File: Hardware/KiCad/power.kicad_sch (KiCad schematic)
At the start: 38 parts, among them U6 TP6841S6, U7 TPS73233

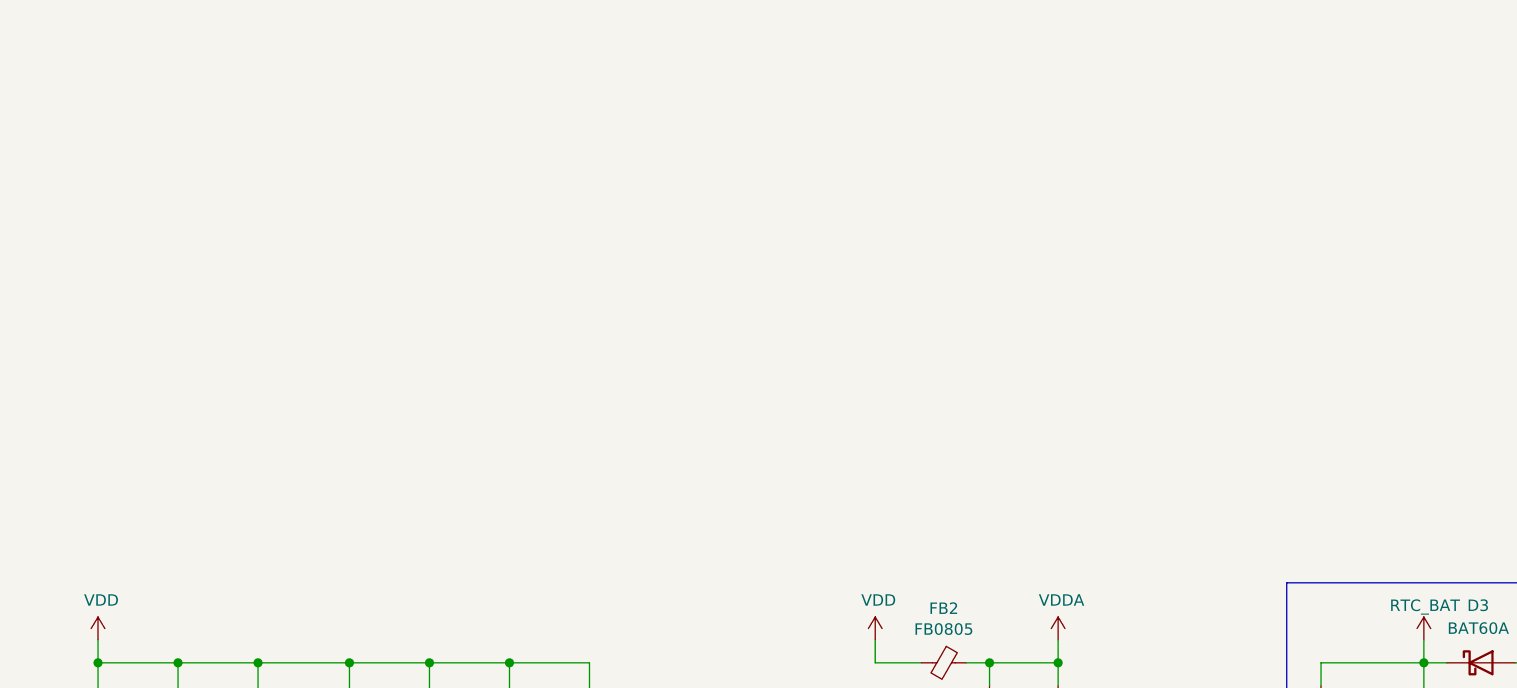
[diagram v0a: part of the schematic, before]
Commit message: Added footprints for decoupling caps
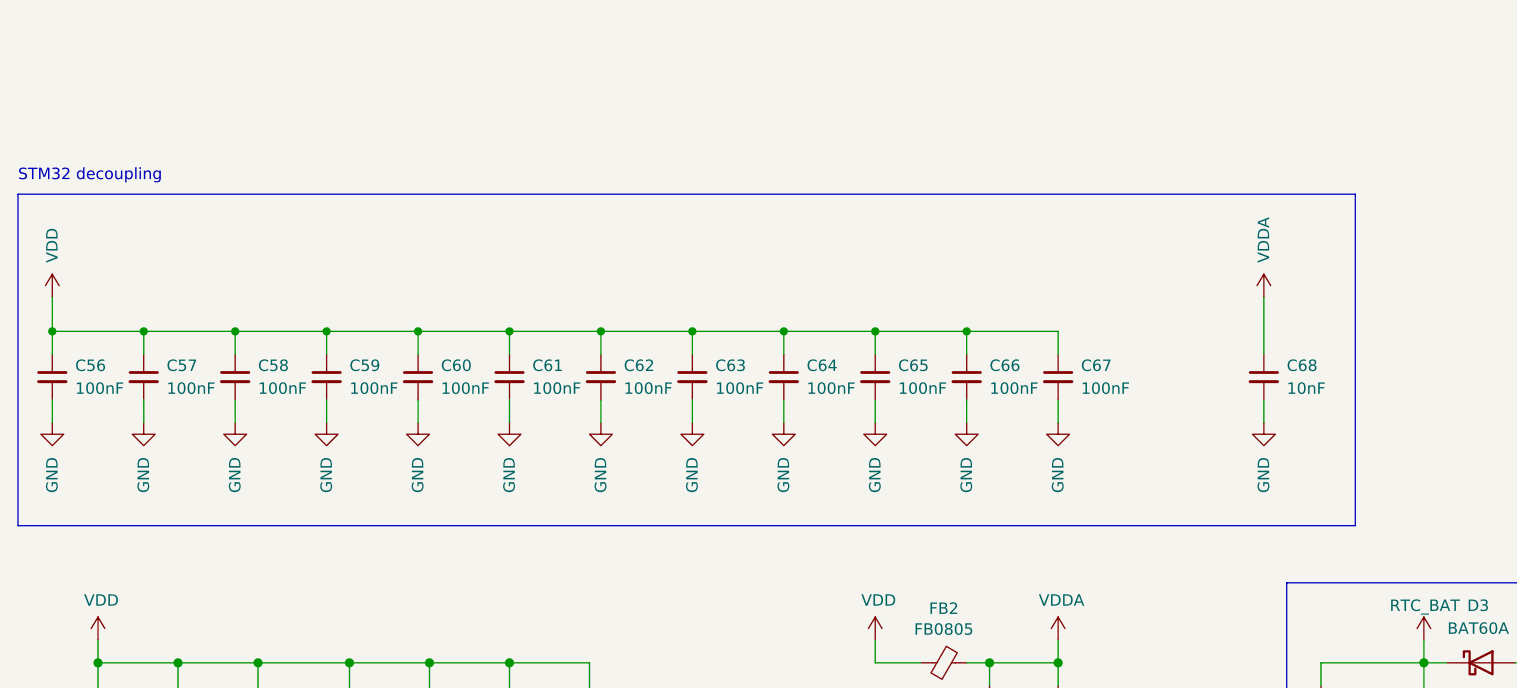
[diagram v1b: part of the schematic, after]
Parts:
- added C56, C57, C58, C59, C60, C61, C62, C63, C64, C65, C66, C67: 100nF, Capacitor_SMD:C_0402_1005Metric, symbol Device:C_Small
- added C68: 10nF, Capacitor_SMD:C_0402_1005Metric, symbol Device:C_Small
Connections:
- net GND: now also C56.2, C57.2, C58.2, C59.2, C60.2, C61.2, C62.2, C63.2, C64.2, C65.2, C66.2, C67.2, C68.2
- net VDD: now also C56.1, C57.1, C58.1, C59.1, C60.1, C61.1, C62.1, C63.1, C64.1, C65.1, C66.1, C67.1
- net VDDA: now also C68.1
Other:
- note added: "STM32 decoupling"

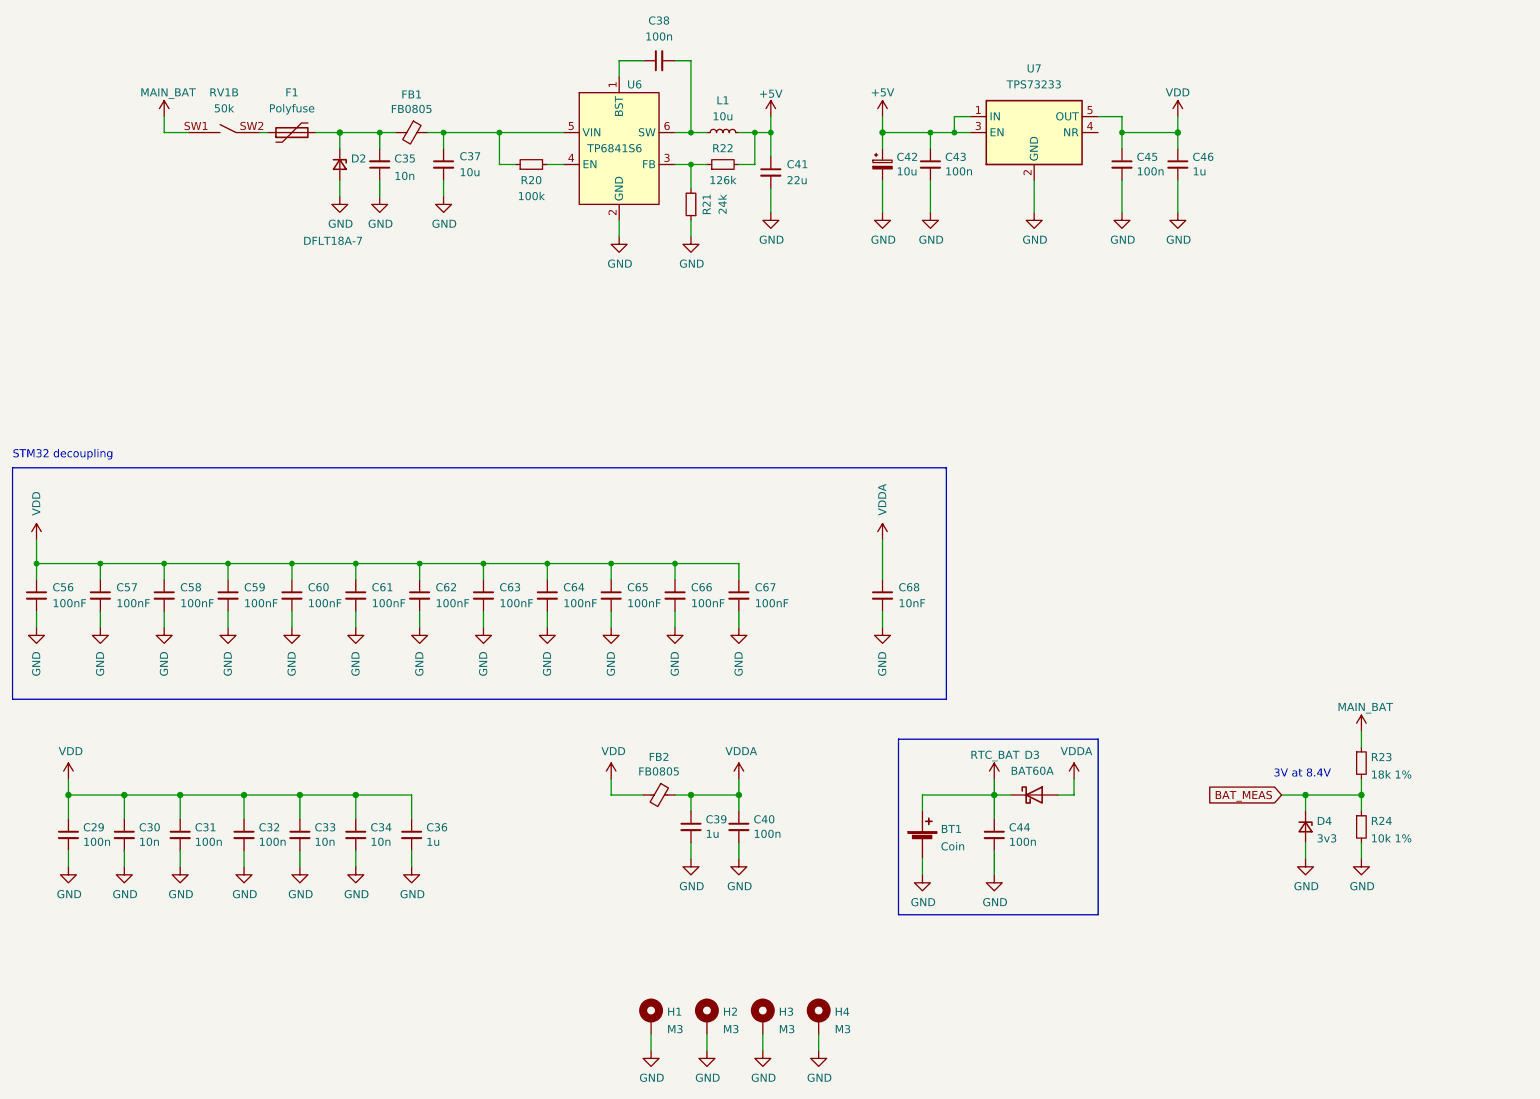
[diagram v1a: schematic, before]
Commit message: Update
- `H*` holes changed to M2
- RTC battery was connected to `VDDA` instead of `VDD`
- added CC1200 decoupling caps
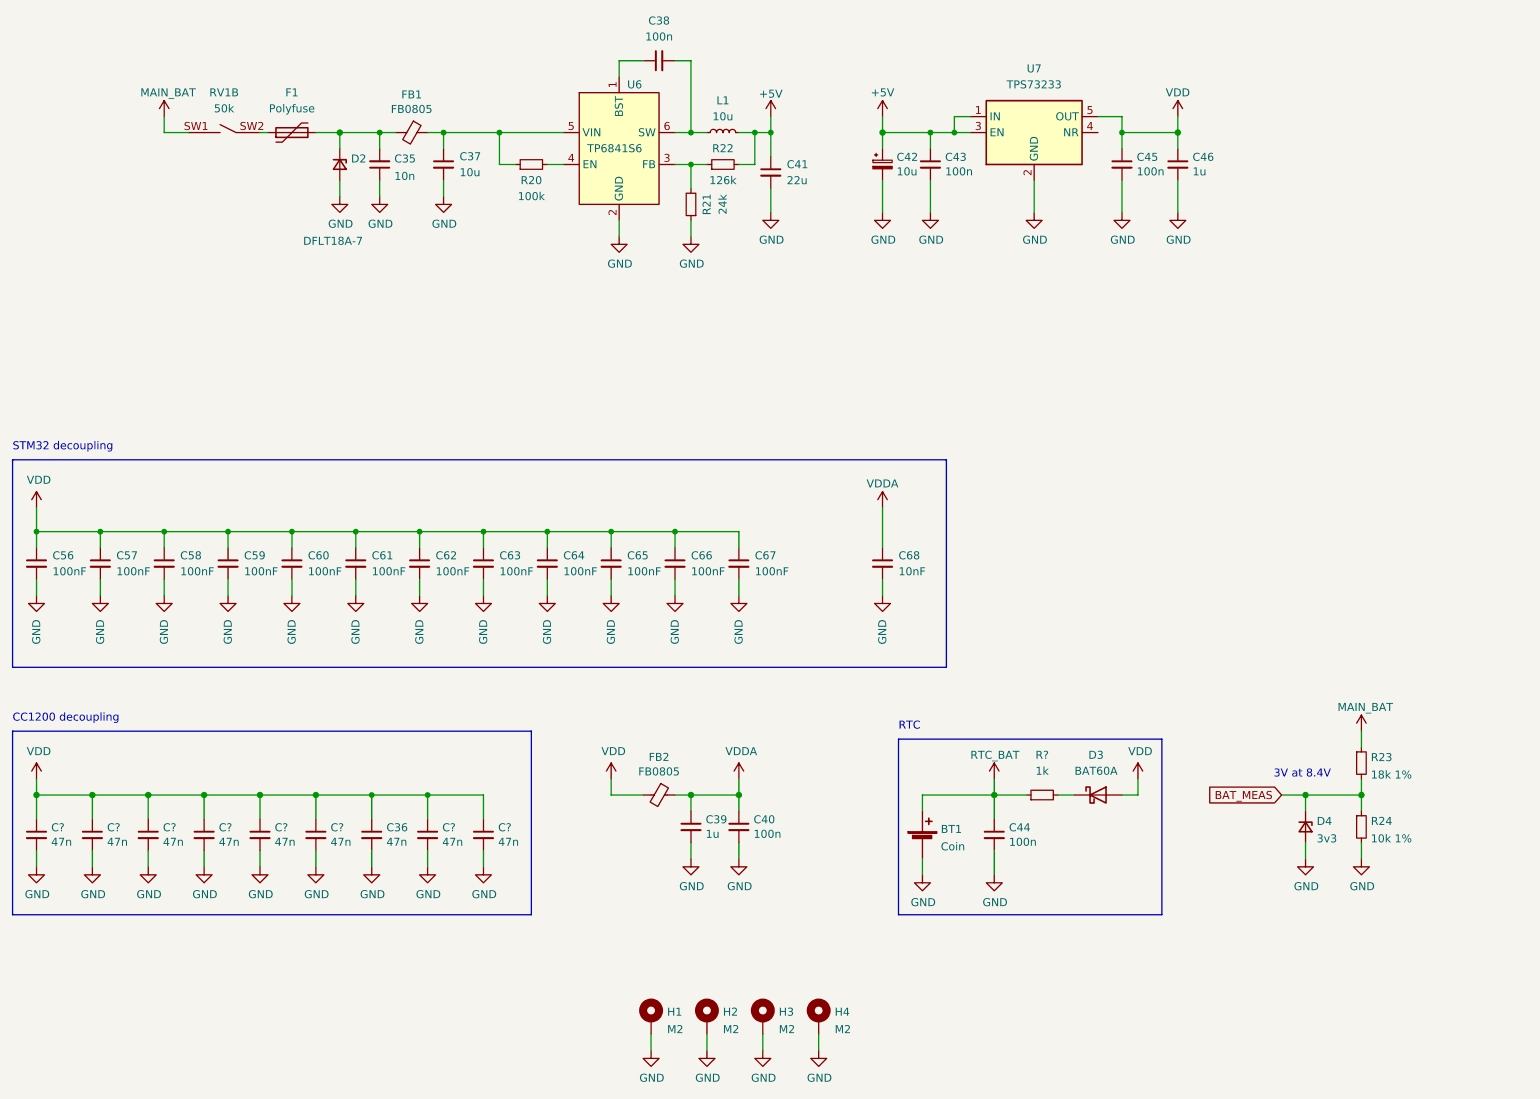
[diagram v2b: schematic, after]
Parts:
- removed C29, C31, C32: 100n, Capacitor_SMD:C_0402_1005Metric, symbol pkl_device:pkl_C_Small
- removed C30, C33, C34: 10n, Capacitor_SMD:C_0402_1005Metric, symbol pkl_device:pkl_C_Small
- added C? (x8): 47n, Capacitor_SMD:C_0402_1005Metric, symbol pkl_device:pkl_C_Small
- added R?: 1k, Resistor_SMD:R_0402_1005Metric, symbol pkl_device:pkl_R_Small
- C36: value 1u -> 47n
- H1, H2, H3, H4: value M3 -> M2; footprint MountingHole:MountingHole_2.7mm_M2.5_DIN965_Pad -> MountingHole:MountingHole_2.2mm_M2_DIN965_Pad
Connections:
- net GND: now also C?.2, C?.2, C?.2, C?.2, C?.2, C?.2, C?.2, C?.2
- net VBAT: now also R?.1; no longer D3.1 (K)
- net VDD: now also D3.2 (A), C?.1, C?.1, C?.1, C?.1, C?.1, C?.1, C?.1, C?.1
- net VDDA: no longer D3.2 (A)
- new net: D3.1 (K), R?.2
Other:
- note added: "CC1200 decoupling"
- note added: "RTC"
- moved on the sheet: C36, C56, C57, C58, C59, C60, C61, C62, C63, C64, C65, C66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

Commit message: adjust footprints
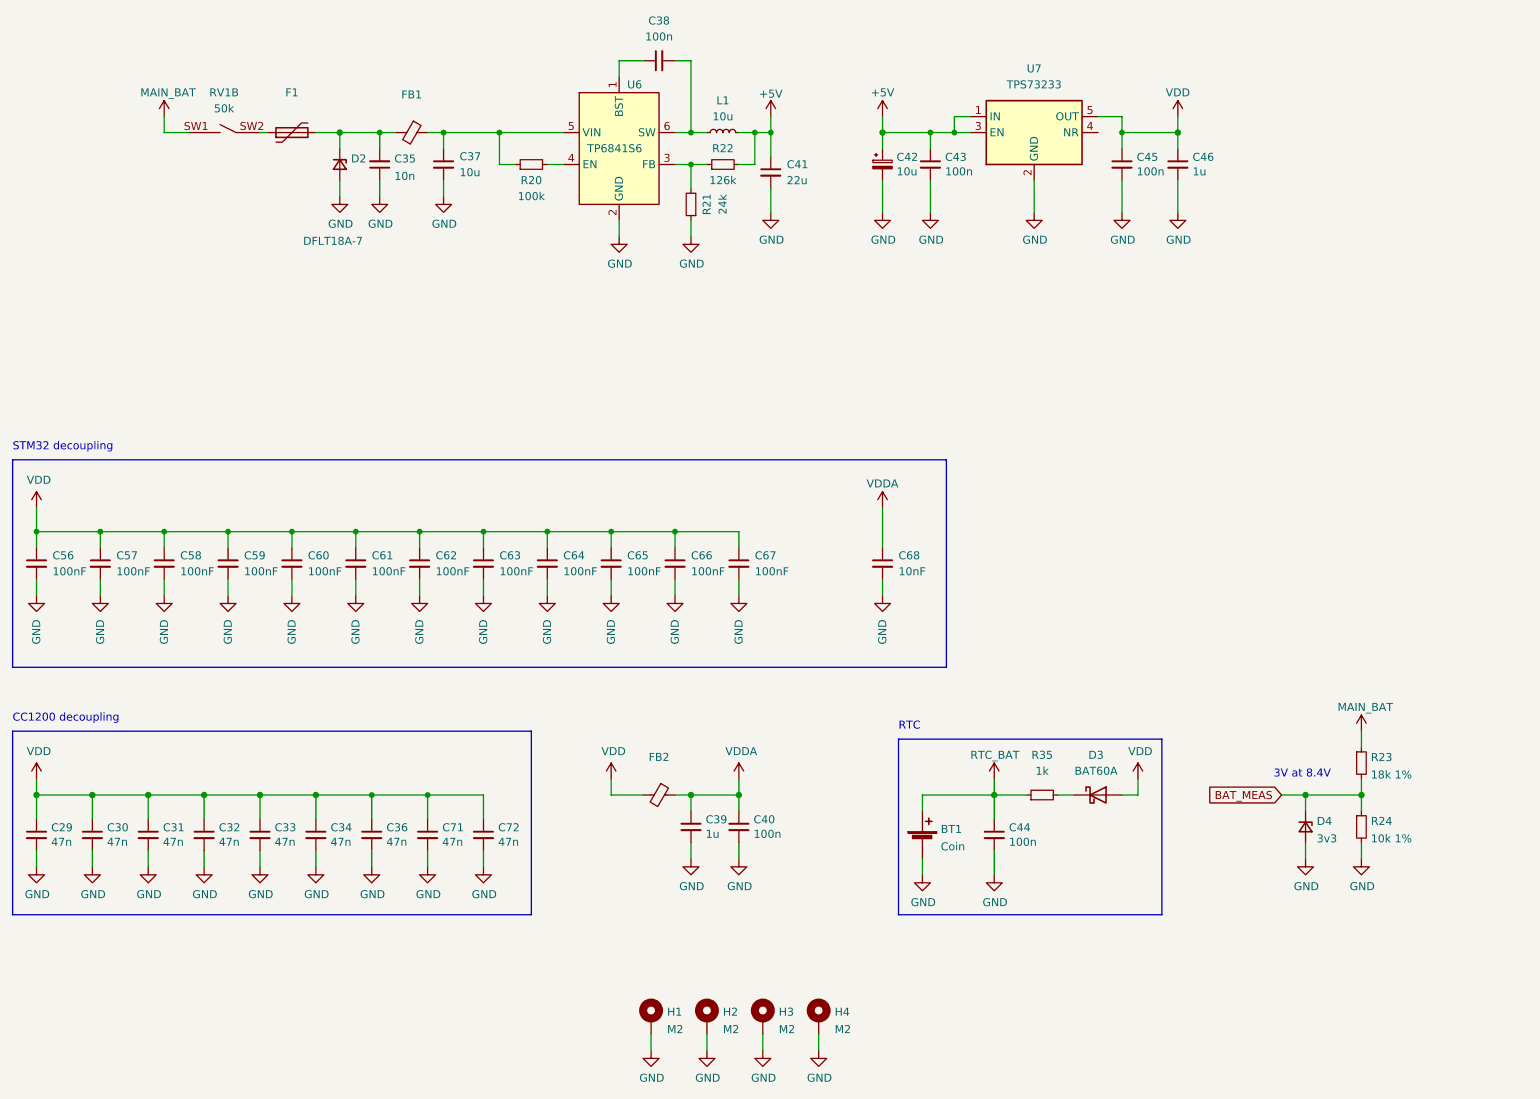
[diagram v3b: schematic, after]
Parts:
- F1: value Polyfuse -> (none); footprint Fuse:Fuse_0805_2012Metric -> (none)
- FB1, FB2: value FB0805 -> (none); footprint pkl_dipol:L_0805 -> (none)
- gave numbers to parts that had none: 9
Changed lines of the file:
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@@
   (symbol (lib_id "pkl_device:pkl_C_Small") (at 41.91 147.32 0) (unit 1)
     (in_bom yes) (on_board yes)
-    (property "Reference" "C?" (id 0) (at 44.2468 146.1516 0)
+    (property "Reference" "C30" (id 0) (at 44.2468 146.1516 0)
       (effects (font (size 1.27 1.27)) (justify left))
     )
@@
   (symbol (lib_id "pkl_device:pkl_C_Small") (at 50.8 147.32 0) (unit 1)
     (in_bom yes) (on_board yes)
-    (property "Reference" "C?" (id 0) (at 53.1368 146.1516 0)
+    (property "Reference" "C31" (id 0) (at 53.1368 146.1516 0)
       (effects (font (size 1.27 1.27)) (justify left))
     )
@@
   (symbol (lib_id "pkl_device:pkl_C_Small") (at 68.58 147.32 0) (unit 1)
     (in_bom yes) (on_board yes)
-    (property "Reference" "C?" (id 0) (at 70.9168 146.1516 0)
+    (property "Reference" "C33" (id 0) (at 70.9168 146.1516 0)
       (effects (font (size 1.27 1.27)) (justify left))
     )
@@
   (symbol (lib_id "power:GND") (at 104.14 152.4 0) (unit 1)
     (in_bom yes) (on_board yes)
-    (property "Reference" "#PWR?" (id 0) (at 104.14 158.75 0)
+    (property "Reference" "#PWR0208" (id 0) (at 104.14 158.75 0)
       (effects (font (size 1.27 1.27)) hide)
     )
@@
     (in_bom yes) (on_board yes)
     (property "Reference" "FB1" (id 0) (at 92.71 29.5402 90))
-    (property "Value" "FB0805" (id 1) (at 92.71 31.8516 90))
-    (property "Footprint" "pkl_dipol:L_0805" (id 2) (at 92.71 33.782 90)
+    (property "Value" "" (id 1) (at 92.71 31.8516 90))
+    (property "Footprint" "" (id 2) (at 92.71 33.782 90)
       (effects (font (size 1.27 1.27)) hide)
     )
@@
   (symbol (lib_id "pkl_device:pkl_C_Small") (at 77.47 147.32 0) (unit 1)
     (in_bom yes) (on_board yes)
-    (property "Reference" "C?" (id 0) (at 79.8068 146.1516 0)
+    (property "Reference" "C34" (id 0) (at 79.8068 146.1516 0)
       (effects (font (size 1.27 1.27)) (justify left))
     )
@@
   (symbol (lib_id "pkl_device:pkl_R_Small") (at 193.04 140.97 90) (unit 1)
     (in_bom yes) (on_board yes) (fields_autoplaced)
-    (property "Reference" "R?" (id 0) (at 193.04 134.62 90))
+    (property "Reference" "R35" (id 0) (at 193.04 134.62 90))
     (property "Value" "1k" (id 1) (at 193.04 137.16 90))
     (property "Footprint" "Resistor_SMD:R_0402_1005Metric" (id 2) (at 193.04 140.97 0)
@@
   (symbol (lib_id "power:VDD") (at 33.02 95.25 0) (unit 1)
     (in_bom yes) (on_board yes)
-    (property "Reference" "#PWR?" (id 0) (at 33.02 99.06 0)
+    (property "Reference" "#PWR0222" (id 0) (at 33.02 99.06 0)
       (effects (font (size 1.27 1.27)) hide)
     )
@@
   (symbol (lib_id "power:GND") (at 95.25 152.4 0) (unit 1)
     (in_bom yes) (on_board yes)
-    (property "Reference" "#PWR?" (id 0) (at 95.25 158.75 0)
+    (property "Reference" "#PWR0221" (id 0) (at 95.25 158.75 0)
       (effects (font (size 1.27 1.27)) hide)
     )
@@
     (in_bom yes) (on_board yes) (fields_autoplaced)
     (property "Reference" "F1" (id 0) (at 73.66 29.21 90))
-    (property "Value" "Polyfuse" (id 1) (at 73.66 31.75 90))
-    (property "Footprint" "Fuse:Fuse_0805_2012Metric" (id 2) (at 78.74 34.29 0)
+    (property "Value" "" (id 1) (at 73.66 31.75 90))
+    (property "Footprint" "" (id 2) (at 78.74 34.29 0)
       (effects (font (size 1.27 1.27)) (justify left) hide)
     )
@@
   (symbol (lib_id "power:VDD") (at 208.28 138.43 0) (unit 1)
     (in_bom yes) (on_board yes)
-    (property "Reference" "#PWR?" (id 0) (at 208.28 142.24 0)
+    (property "Reference" "#PWR0186" (id 0) (at 208.28 142.24 0)
       (effects (font (size 1.27 1.27)) hide)
     )
@@
     (in_bom yes) (on_board yes)
     (property "Reference" "FB2" (id 0) (at 132.08 134.9502 90))
-    (property "Value" "FB0805" (id 1) (at 132.08 137.2616 90))
-    (property "Footprint" "pkl_dipol:L_0805" (id 2) (at 132.08 139.192 90)
+    (property "Value" "" (id 1) (at 132.08 137.2616 90))
+    (property "Footprint" "" (id 2) (at 132.08 139.192 90)
       (effects (font (size 1.27 1.27)) hide)
     )
@@
   (symbol (lib_id "pkl_device:pkl_C_Small") (at 59.69 147.32 0) (unit 1)
     (in_bom yes) (on_board yes)
-    (property "Reference" "C?" (id 0) (at 62.0268 146.1516 0)
+    (property "Reference" "C32" (id 0) (at 62.0268 146.1516 0)
       (effects (font (size 1.27 1.27)) (justify left))
     )
@@
   (symbol (lib_id "pkl_device:pkl_C_Small") (at 104.14 147.32 0) (unit 1)
     (in_bom yes) (on_board yes)
-    (property "Reference" "C?" (id 0) (at 106.4768 146.1516 0)
+    (property "Reference" "C72" (id 0) (at 106.4768 146.1516 0)
       (effects (font (size 1.27 1.27)) (justify left))
     )
@@
   (symbol (lib_id "pkl_device:pkl_C_Small") (at 95.25 147.32 0) (unit 1)
     (in_bom yes) (on_board yes)
-    (property "Reference" "C?" (id 0) (at 97.5868 146.1516 0)
+    (property "Reference" "C71" (id 0) (at 97.5868 146.1516 0)
       (effects (font (size 1.27 1.27)) (justify left))
     )
@@
   (symbol (lib_id "pkl_device:pkl_C_Small") (at 33.02 147.32 0) (unit 1)
     (in_bom yes) (on_board yes)
-    (property "Reference" "C?" (id 0) (at 35.3568 146.1516 0)
-      (effects (font (size 1.27 1.27)) (justify left))
-    )
+    (property "Reference" "C29" (id 0) (at 35.3568 146.1516 0)
+      (effects (font (size 1.27 1.27)) (justify left))
+    )
